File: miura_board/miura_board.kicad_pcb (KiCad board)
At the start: 4 copper layers, 55.9 x 52.4 mm, 40 parts, among them J1 Micro_SD_Card_Det, J2 Conn_01x04_Male, J4 Conn_01x04_Male, J6 Conn_01x02_Male, SW1 SW_Push, SW2 SW_Push, U1 ESP32-WROOM, U2 AMS1117, U3 CP2102N-Axx-xQFN28, U4 MCP73832-5-OT, U5 AMS1117, U6 MPU-6050

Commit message: Routing done
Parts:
- added C18: 10uF, Capacitor_SMD:C_0603_1608Metric, F.Cu at (108.6, 45.7)
- added C19: 10uF, Capacitor_SMD:C_0603_1608Metric, F.Cu at (107.2, 70.2)
- added C20: 10uF, Capacitor_SMD:C_0603_1608Metric, F.Cu at (107.2, 72.6)
- added D1: LED, Diode_SMD:D_0603_1608Metric, F.Cu at (105.2, 39.8)
- added R5: 4.7K, Resistor_SMD:R_0603_1608Metric, F.Cu at (106.0, 43.0)
- added R6: 4.7K, Resistor_SMD:R_0603_1608Metric, F.Cu at (101.7, 40.6)
- C15, C16, C17, C26, C29, R2: moved to B.Cu
- C3, U2: moved to F.Cu
- J2, J4: footprint Connector_PinHeader_2.54mm:PinHeader_1x04_P2.54mm_Vertical -> Connector_PinHeader_1.27mm:PinHeader_1x04_P1.27mm_Vertical
- moved C14 94.2 mm to (65.7, 60.4), turned to -90 degrees
- moved C17 86.6 mm to (62.7, 65.5), turned to 90 degrees
- moved C13 80.6 mm to (95.9, 75.7), turned to -90 degrees
- moved C7 80.0 mm to (94.5, 68.1)
- moved C10 79.6 mm to (93.9, 75.7), turned to -90 degrees
- moved C16 76.0 mm to (87.9, 55.3)
- moved R1 73.0 mm to (90.8, 71.9), turned to 180 degrees
- moved R2 71.3 mm to (77.6, 54.2), turned to 180 degrees
- moved C29 69.9 mm to (88.6, 64.5)
- moved C15 62.5 mm to (90.6, 60.4), turned to -90 degrees
- moved C11 58.9 mm to (91.9, 75.7), turned to -90 degrees
- moved C4 58.2 mm to (96.0, 45.5), turned to 90 degrees
- moved C26 53.4 mm to (92.6, 60.5), turned to -90 degrees
- moved C12 52.0 mm to (89.9, 75.7), turned to -90 degrees
- moved J2 46.3 mm to (63.5, 72.4), turned to 180 degrees
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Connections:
- J2 pad 4: +3V3 -> MOTOR_SUPPLY
- J4 pad 4: +3V3 -> MOTOR_SUPPLY
- U4 pad 1: unconnected-(U4-Pad1) -> Net-(U4-Pad1)
- U4 pad 2: unconnected-(U4-Pad2) -> GND
- U4 pad 4: unconnected-(U4-Pad4) -> VBUS
- U4 pad 5: unconnected-(U4-Pad5) -> Net-(U4-Pad5)
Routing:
- net GND: track 0.00 -> 135.9 mm, vias 0 -> 25
- net MOTOR_SUPPLY: track 0.00 -> 79.7 mm, vias 0 -> 1
- net RXD0: track 0.00 -> 54.7 mm, vias 0 -> 2
- net TXD0: track 0.00 -> 53.7 mm, vias 0 -> 2
- net VBUS: track 0.00 -> 50.4 mm, vias 0 -> 2
- net +3V3: track 0.00 -> 48.3 mm, vias 0 -> 7
- net SCL: track 0.00 -> 24.8 mm, vias 0 -> 1
- net VBAT: track 0.00 -> 24.7 mm
- net MOSI: track 0.00 -> 22.3 mm, vias 0 -> 1
- net Net-(C7-Pad1): track 0.00 -> 20.2 mm
- net SDA: track 0.00 -> 20.1 mm, vias 0 -> 1
- net Net-(C14-Pad1): track 0.00 -> 13.6 mm
- net CS: track 0.00 -> 10.8 mm, vias 0 -> 1
- net Net-(R3-Pad1): track 0.00 -> 10.2 mm
- net Net-(R4-Pad1): track 0.00 -> 9.13 mm
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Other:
- board text added: "Miura Bot"

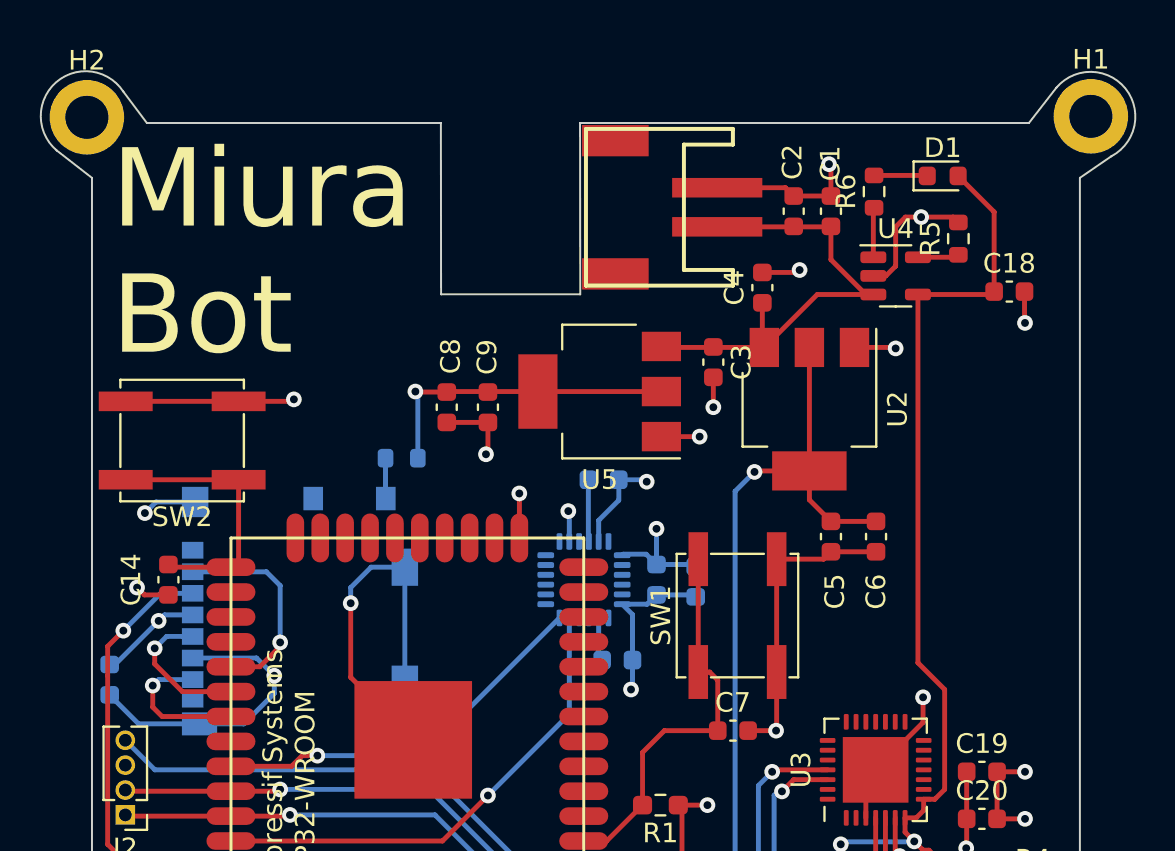
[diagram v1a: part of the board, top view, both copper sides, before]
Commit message: Added switch
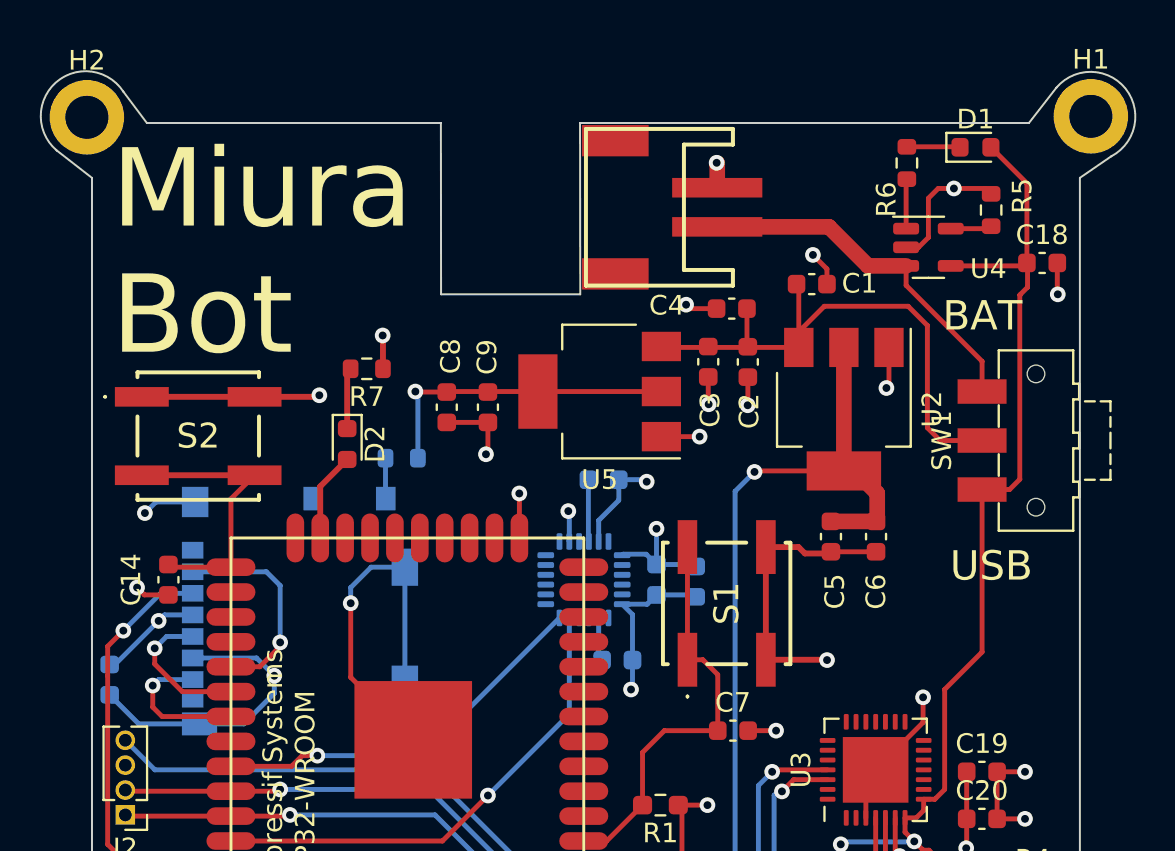
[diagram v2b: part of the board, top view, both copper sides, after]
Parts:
- removed SW2: SW_Push, Button_Switch_SMD:SW_SPST_EVPBF
- added D2: LED, Diode_SMD:D_0603_1608Metric, F.Cu at (74.8, 53.5)
- added R7: 4.7K, Resistor_SMD:R_0603_1608Metric, F.Cu at (75.8, 49.6)
- added S1: EVP-BV4C3L000, EVPBVC_TactileSw:EVPBV4C3L000, F.Cu at (94.2, 61.6)
- added S2: EVP-BV4C3L000, EVPBVC_TactileSw:EVPBV4C3L000, F.Cu at (67.2, 53.1)
- SW1: value SW_Push -> SW_SPDT; footprint Button_Switch_SMD:SW_SPST_EVPBF -> Button_Switch_SMD:SW_SPDT_CK-JS102011SAQN
- moved SW1 17.7 mm to (110.0, 53.3)
- moved C2 8.04 mm to (95.3, 49.3), turned to -90 degrees
- moved C1 3.85 mm to (98.5, 45.3), turned to 0 degrees
- moved C18 2.22 mm to (110.3, 44.2)
- moved R5 2.22 mm to (107.7, 41.5)
- moved R6 2.22 mm to (103.4, 39.1)
- moved U4 2.22 mm to (104.5, 43.4)
- moved D1 2.22 mm to (106.9, 38.3)
- moved C4 1.89 mm to (94.4, 46.6), turned to 180 degrees
- moved U2 1.76 mm to (100.2, 51.7)
- moved C3 0.26 mm to (93.2, 49.3)
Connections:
- C1 pad 1: VBAT -> VIN
- C2 pad 1: VBAT -> VIN
- C3 pad 1: VBAT -> VIN
- C4 pad 1: VBAT -> VIN
- C7 pad 2: GND -> unconnected-(C7-Pad2)
- SW1 pad 1: Net-(C7-Pad1) -> VBUS
- SW1 pad 2: GND -> VIN
- U1 pad 10: MOTOR_A31_IN -> unconnected-(U1-Pad10)
- U1 pad 11: MOTOR_A32_IN -> unconnected-(U1-Pad11)
- U1 pad 12: MOTOR_B31_IN -> unconnected-(U1-Pad12)
- U1 pad 13: MOTOR_B32_IN -> unconnected-(U1-Pad13)
- U1 pad 14: MOTOR_B11_IN -> unconnected-(U1-Pad14)
- U1 pad 16: MOTOR_B12_IN -> unconnected-(U1-Pad16)
- U1 pad 23: MOTOR_A12_IN -> toggle
- U1 pad 24: MOTOR_A11_IN -> unconnected-(U1-Pad24)
- U1 pad 6: MOTOR_A22_IN -> unconnected-(U1-Pad6)
- U1 pad 7: MOTOR_A21_IN -> unconnected-(U1-Pad7)
- U1 pad 8: MOTOR_B22_IN -> unconnected-(U1-Pad8)
- U1 pad 9: MOTOR_B21_IN -> unconnected-(U1-Pad9)
- U2 pad 3: VBAT -> VIN
- U5 pad 3: VBAT -> VIN
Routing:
- net VIN: track 0.00 -> 28.9 mm
- net VBAT: track 24.7 -> 19.3 mm
- net toggle: track 0.00 -> 4.57 mm
- net VBUS: track 50.4 -> 54.0 mm
- net Net-(D2-Pad1): track 0.00 -> 3.12 mm
- net GND: track 135.9 -> 133.7 mm, vias 25 -> 28
- net unconnected-(C7-Pad2): track 0.00 -> 1.47 mm, vias 0 -> 1
- net Net-(C7-Pad1): track 20.2 -> 21.2 mm
- net MOTOR_SUPPLY: track 79.7 -> 80.3 mm
- net Net-(C14-Pad1): track 13.6 -> 14.2 mm
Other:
- board text added: "BAT"
- board text added: "USB"

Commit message: Order ready
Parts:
- removed J4: Conn_01x04_Male, Connector_PinHeader_1.27mm:PinHeader_1x04_P1.27mm_Vertical
- added J3: Conn_01x05_Female, Connector_PinHeader_1.27mm:PinHeader_1x05_P1.27mm_Vertical, F.Cu at (95.2, 82.6)
- J2: value Conn_01x04_Male -> Conn_01x05_Female; footprint Connector_PinHeader_1.27mm:PinHeader_1x04_P1.27mm_Vertical -> Connector_PinHeader_1.27mm:PinHeader_1x05_P1.27mm_Vertical
- moved C17 6.94 mm to (66.8, 71.1)
- moved J2 2.45 mm to (63.5, 74.8)
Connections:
- J2 pad 1: TXD0 -> +3V3
- J2 pad 2: RXD0 -> MOTOR_SUPPLY
- J2 pad 4: MOTOR_SUPPLY -> SCL
- J6 pad 1: GND -> VBAT
- J6 pad 2: VBAT -> GND
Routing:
- net SDA: track 20.1 -> 52.3 mm
- net SCL: track 24.8 -> 49.6 mm
- net RXD0: track 54.7 -> 30.9 mm
- net TXD0: track 53.7 -> 31.4 mm
- net +3V3: track 48.3 -> 63.6 mm, vias 7 -> 6
- net MOSI: track 22.3 -> 24.9 mm
- net GND: track 133.7 -> 132.1 mm
- net VBAT: track 19.3 -> 20.1 mm
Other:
- board text added: "3v3"
- board text added: "GND"
- board text added: "M+"
- board text added: "SCL"
- board text added: "SDA"
